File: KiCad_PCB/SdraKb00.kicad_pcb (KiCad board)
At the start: 2 copper layers, 85.3 x 83.4 mm, 75 parts, among them J1 AVR-ISP-6, SW00 SW_Push_45deg, SW01 SW_Push_45deg, SW02 SW_Push_45deg, SW03 RotaryEncoder_Switch, SW10 SW_Push_45deg, SW11 SW_Push_45deg, SW12 SW_Push_45deg, SW13 SW_Push_45deg, SW20 SW_Push_45deg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

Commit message: Finilizing PCB design.
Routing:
- net VCC: track 15.9 -> 20.6 mm
- net GND: track 108.5 -> 110.4 mm, vias 38 -> 40

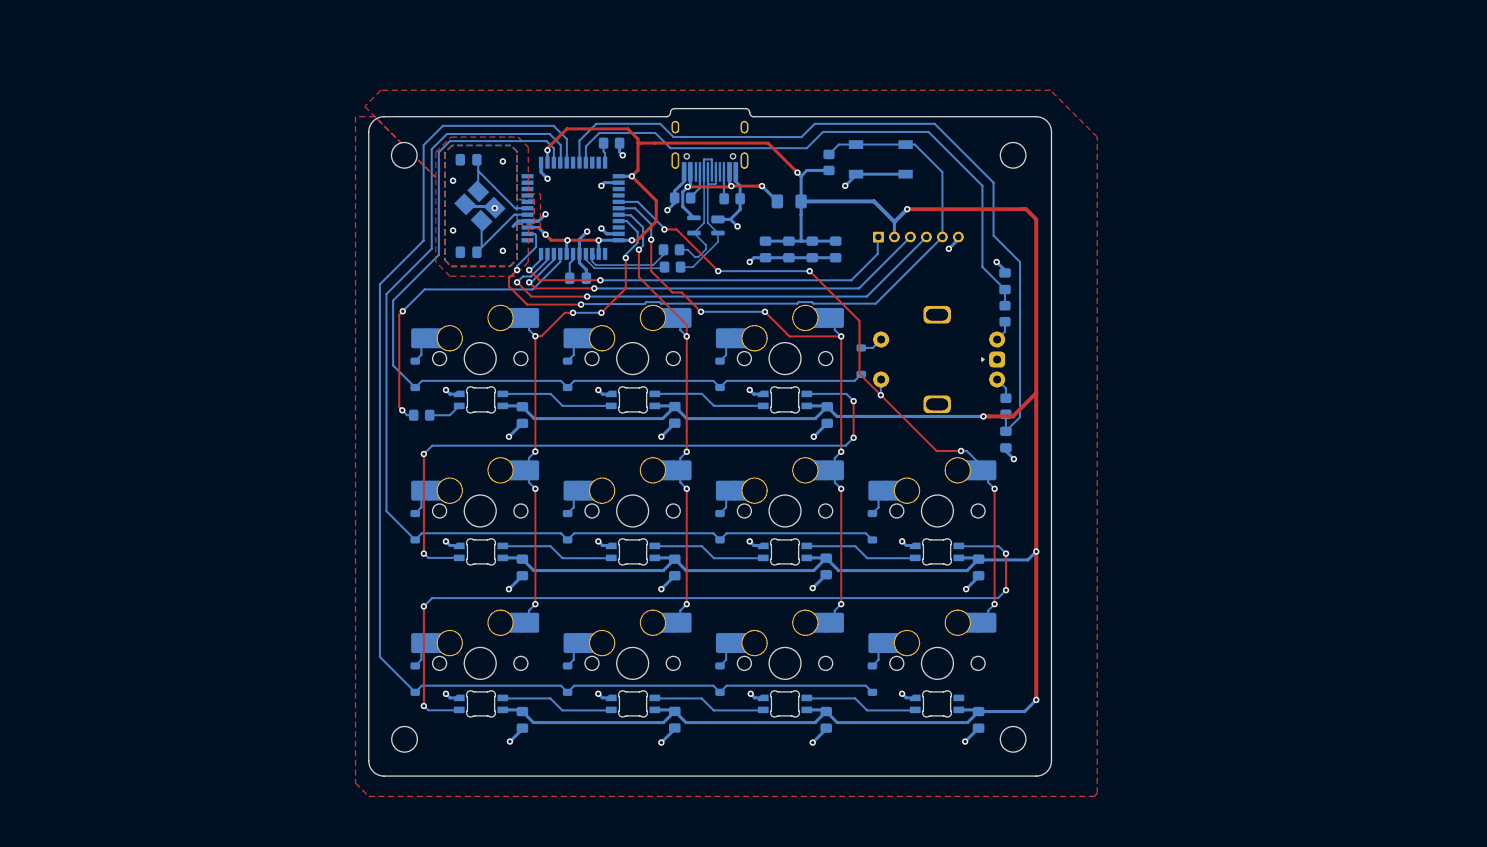
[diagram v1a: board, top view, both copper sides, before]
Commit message: Silkscreen (#5)
* Adding initial silkscreen.

* Adding KiCad & OpenHW logos.
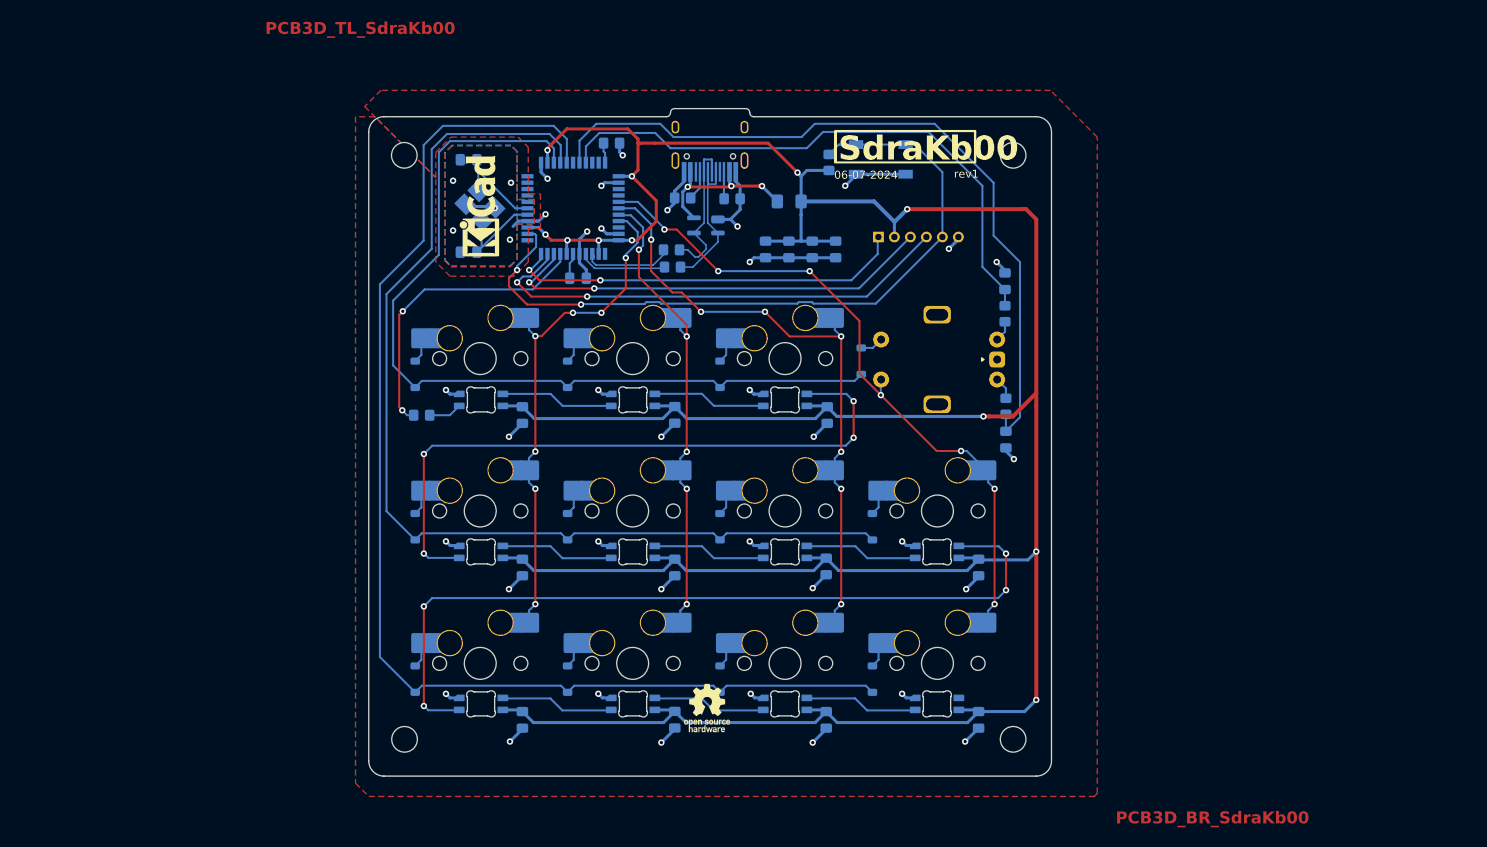
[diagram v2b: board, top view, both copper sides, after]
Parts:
- added REF**: KiCad-Logo_5mm_SilkScreen, Symbol:KiCad-Logo_5mm_SilkScreen, F.Cu at (115.4, 73.9)
- added REF**: OSHW-Logo_5.7x6mm_SilkScreen, Symbol:OSHW-Logo_5.7x6mm_SilkScreen, F.Cu at (143.4, 136.7)
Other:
- board text added: "06-07-2024"
- board text added: "PCB3D_BR_SdraKb00"
- board text added: "PCB3D_TL_SdraKb00"
- board text added: "SdraKb00"
- board text added: "rev1"

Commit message: Adding PCB renders.
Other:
- board text removed: "PCB3D_BR_SdraKb00"
- board text removed: "PCB3D_TL_SdraKb00"
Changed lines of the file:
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@@
 		(fp_arc
 			(start 1.749484 0.919719)
-			(mid 1.712541 0.814065)
+			(mid 1.712534 0.814065)
 			(end 1.699999 0.702841)
 			(stroke
@@
 		(fp_arc
 			(start 1.699999 -0.702844)
-			(mid 1.712538 -0.814067)
+			(mid 1.712537 -0.814067)
 			(end 1.749484 -0.919721)
 			(stroke
@@
 		(fp_arc
 			(start 1.749484 0.919719)
-			(mid 1.712534 0.814065)
+			(mid 1.712541 0.814065)
 			(end 1.699999 0.702841)
 			(stroke
@@
 		(fp_arc
 			(start 1.699999 -0.702844)
-			(mid 1.712537 -0.814067)
+			(mid 1.712538 -0.814067)
 			(end 1.749484 -0.919721)
 			(stroke
@@
 		(fp_arc
 			(start 1.749484 0.919719)
-			(mid 1.712541 0.814065)
+			(mid 1.712534 0.814065)
 			(end 1.699999 0.702841)
 			(stroke
@@
 		(fp_arc
 			(start 1.699999 -0.702844)
-			(mid 1.712538 -0.814067)
+			(mid 1.712537 -0.814067)
 			(end 1.749484 -0.919721)
 			(stroke
@@
 		(fp_arc
 			(start 1.749484 0.919719)
-			(mid 1.712534 0.814065)
+			(mid 1.712541 0.814065)
 			(end 1.699999 0.702841)
 			(stroke
@@
 		(fp_arc
 			(start 1.699999 -0.702844)
-			(mid 1.712537 -0.814067)
+			(mid 1.712538 -0.814067)
 			(end 1.749484 -0.919721)
 			(stroke
@@
 		(fp_arc
 			(start 1.749484 0.919719)
-			(mid 1.712541 0.814065)
+			(mid 1.712534 0.814065)
 			(end 1.699999 0.702841)
 			(stroke
@@
 		(fp_arc
 			(start 1.699999 -0.702844)
-			(mid 1.712538 -0.814067)
+			(mid 1.712537 -0.814067)
 			(end 1.749484 -0.919721)
 			(stroke
@@
 		(fp_arc
 			(start 1.749484 0.919719)
-			(mid 1.712541 0.814065)
+			(mid 1.712534 0.814065)
 			(end 1.699999 0.702841)
 			(stroke
@@
 		(fp_arc
 			(start 1.699999 -0.702844)
-			(mid 1.712538 -0.814067)
+			(mid 1.712537 -0.814067)
 			(end 1.749484 -0.919721)
 			(stroke
@@
 		(fp_arc
 			(start 1.749484 0.919719)
-			(mid 1.712541 0.814065)
+			(mid 1.712534 0.814065)
 			(end 1.699999 0.702841)
 			(stroke
@@
 		(fp_arc
 			(start 1.699999 -0.702844)
-			(mid 1.712538 -0.814067)
+			(mid 1.712537 -0.814067)
 			(end 1.749484 -0.919721)
 			(stroke
@@
 		(fp_arc
 			(start 1.749484 0.919719)
-			(mid 1.712541 0.814065)
+			(mid 1.712534 0.814065)
 			(end 1.699999 0.702841)
 			(stroke
@@
 		(fp_arc
 			(start 1.699999 -0.702844)
-			(mid 1.712538 -0.814067)
+			(mid 1.712537 -0.814067)
 			(end 1.749484 -0.919721)
 			(stroke
@@
 		(fp_arc
 			(start 1.749484 0.919719)
-			(mid 1.712534 0.814065)
+			(mid 1.712541 0.814065)
 			(end 1.699999 0.702841)
 			(stroke
@@
 		(fp_arc
 			(start 1.699999 -0.702844)
-			(mid 1.712537 -0.814067)
+			(mid 1.712538 -0.814067)
 			(end 1.749484 -0.919721)
 			(stroke
@@
 		(fp_arc
 			(start 1.749484 0.919719)
-			(mid 1.712541 0.814065)
+			(mid 1.712534 0.814065)
 			(end 1.699999 0.702841)
 			(stroke
@@
 		(fp_arc
 			(start 1.699999 -0.702844)
-			(mid 1.712538 -0.814067)
+			(mid 1.712537 -0.814067)
 			(end 1.749484 -0.919721)
 			(stroke
@@
 		(fp_arc
 			(start 1.749484 0.919719)
-			(mid 1.712541 0.814065)
+			(mid 1.712534 0.814065)
 			(end 1.699999 0.702841)
 			(stroke
@@
 		(fp_arc
 			(start 1.699999 -0.702844)
-			(mid 1.712538 -0.814067)
+			(mid 1.712537 -0.814067)
 			(end 1.749484 -0.919721)
 			(stroke
@@
 		(layer "Edge.Cuts")
 	)
-	(gr_text "PCB3D_BR_SdraKb00"
-		(at 194.437 151.257 0)
-		(layer "F.Cu")
-		(effects
-			(font
-				(size 1.5 1.5)
-				(thickness 0.3)
-				(bold yes)
-			)
-			(justify left bottom)
-		)
-	)
-	(gr_text "PCB3D_TL_SdraKb00"
-		(at 88.138 52.578 0)
-		(layer "F.Cu")
-		(effects
-			(font
-				(size 1.5 1.5)
-				(thickness 0.3)
-				(bold yes)
-			)
-			(justify left bottom)
-		)
-	)
 	(gr_text "SdraKb00"

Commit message: Adding power indicator LED (#7)
* Adding power indicator LED.

* Re-placing silkscreen.
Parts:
- removed the REF** at (115.4, 73.9)
- removed the REF** at (143.4, 136.7)
- added D4: RED 1.8V, LED_SMD:LED_1206_3216Metric_Pad1.42x1.75mm_HandSolder, F.Cu at (160.7, 67.1)
- added R10: 640, Resistor_SMD:R_0805_2012Metric_Pad1.20x1.40mm_HandSolder, F.Cu at (157.2, 66.5)
- added REF**: KiCad-Logo2_5mm_SilkScreen, Symbol:KiCad-Logo2_5mm_SilkScreen, F.Cu at (114.9, 73.8)
- added REF**: OSHW-Logo2_9.8x8mm_SilkScreen, Symbol:OSHW-Logo2_9.8x8mm_SilkScreen, F.Cu at (172.0, 68.1)
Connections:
- U1 pad 36: unconnected-(U1-PF7-Pad36) -> STATUS_LED
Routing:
- net +5V: track 418.6 -> 422.1 mm
- net Net-(D4-A): track 0.00 -> 3.44 mm

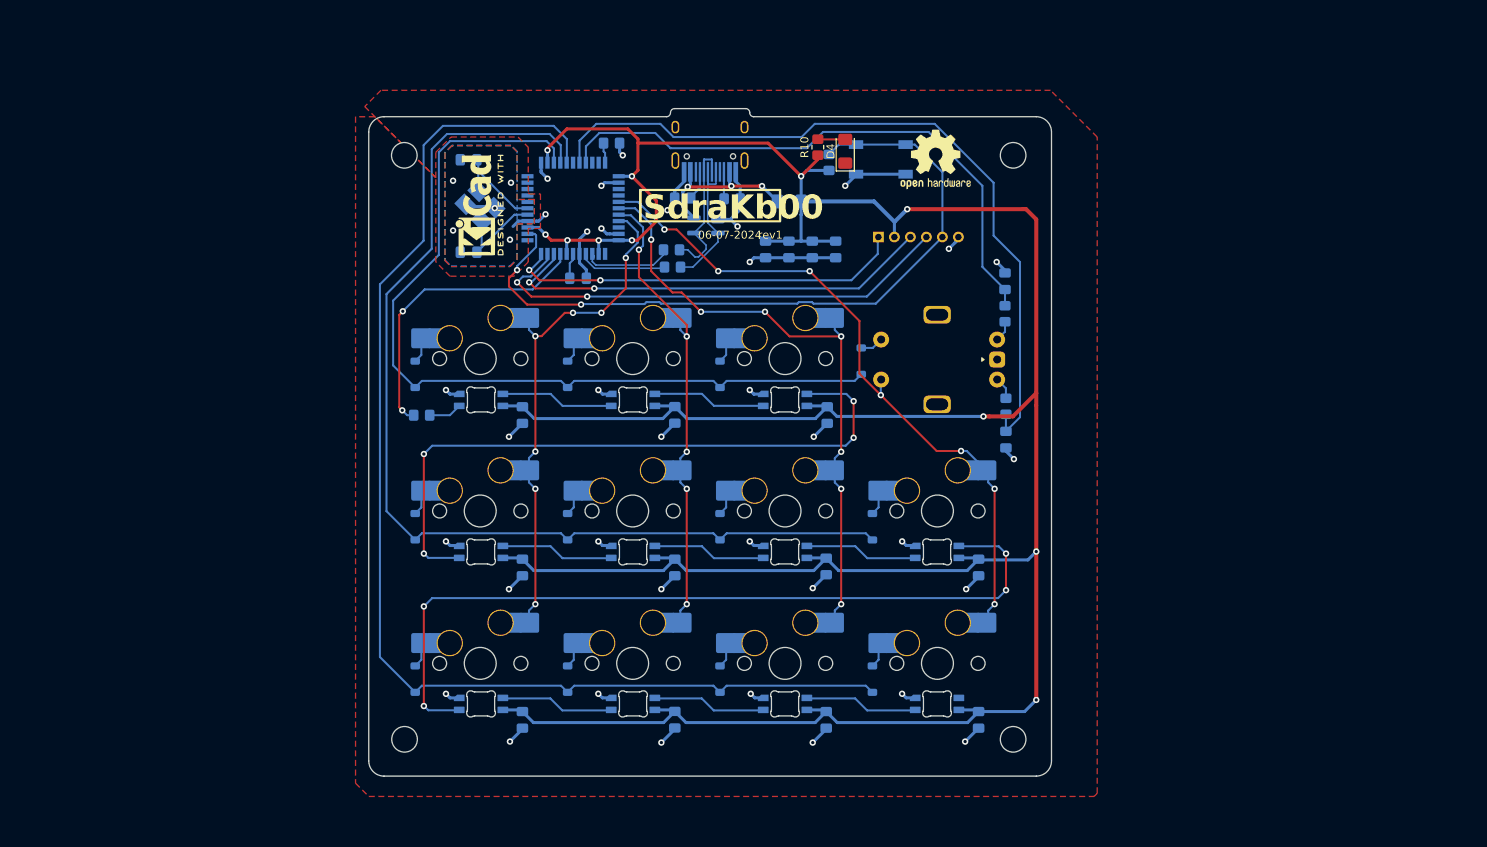
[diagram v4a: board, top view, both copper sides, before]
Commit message: Mounting plate (#8)
* Adding power indicator LED.

* Re-placing silkscreen.

* Adding switch mounting plate.
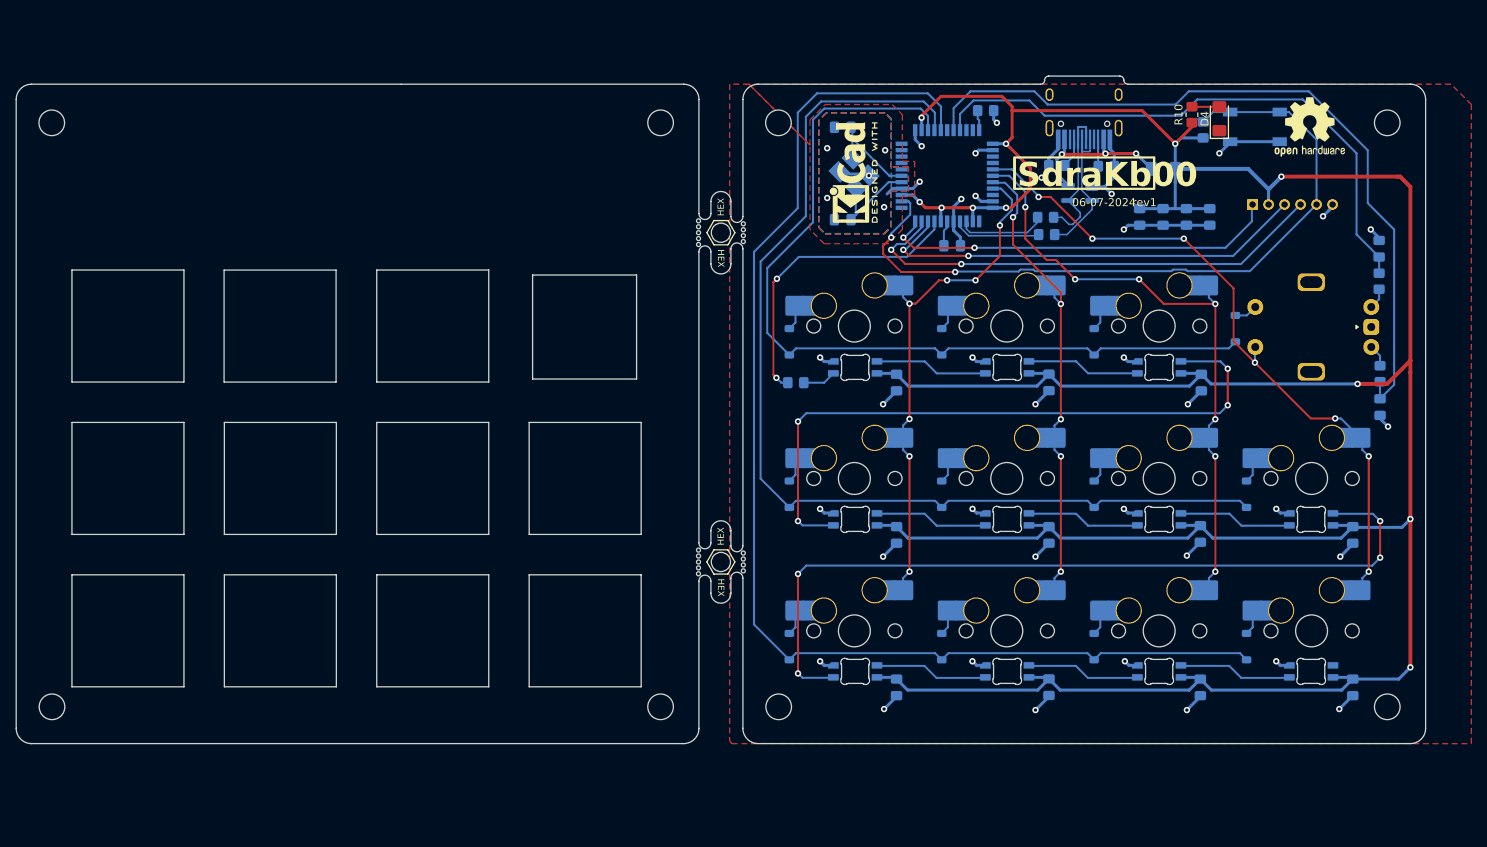
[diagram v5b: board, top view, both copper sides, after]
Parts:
- added H1: MountingHole, MountingHole:MountingHole_3.2mm_M3, F.Cu at (61.5, 136.5)
- added H2: MountingHole, MountingHole:MountingHole_3.2mm_M3, F.Cu at (137.6, 63.5)
- added H3: MountingHole, MountingHole:MountingHole_3.2mm_M3, F.Cu at (61.5, 63.5)
- added H4: MountingHole, MountingHole:MountingHole_3.2mm_M3, F.Cu at (137.6, 136.5)
- added MB5: 5.5mm, marbastlib-various:mousebites_5p5mm_easysnap, F.Cu at (147.9, 118.4)
- added MB5: 5.5mm, marbastlib-various:mousebites_5p5mm_easysnap, F.Cu at (147.9, 77.2)
- added SW01: SW_Push_45deg, marbastlib-mx:SW_MX_HS_CPG151101S11_1u, B.Cu at (90.0, 88.9)
- added SW01: SW_Push_45deg, marbastlib-mx:SW_MX_HS_CPG151101S11_1u, B.Cu at (71.0, 88.9)
- added SW01: SW_Push_45deg, marbastlib-mx:SW_MX_HS_CPG151101S11_1u, B.Cu at (90.0, 108.0)
- added SW01: SW_Push_45deg, marbastlib-mx:SW_MX_HS_CPG151101S11_1u, B.Cu at (71.0, 127.0)
- added SW01: SW_Push_45deg, marbastlib-mx:SW_MX_HS_CPG151101S11_1u, B.Cu at (109.1, 88.9)
- added SW01: SW_Push_45deg, marbastlib-mx:SW_MX_HS_CPG151101S11_1u, B.Cu at (109.1, 127.0)
- added SW01: SW_Push_45deg, marbastlib-mx:SW_MX_HS_CPG151101S11_1u, B.Cu at (128.1, 127.0)
- added SW01: SW_Push_45deg, marbastlib-mx:SW_MX_HS_CPG151101S11_1u, B.Cu at (109.1, 108.0)
- added SW01: SW_Push_45deg, marbastlib-mx:SW_MX_HS_CPG151101S11_1u, B.Cu at (71.0, 108.0)
- added SW01: SW_Push_45deg, marbastlib-mx:SW_MX_HS_CPG151101S11_1u, B.Cu at (90.0, 127.0)
- added SW01: SW_Push_45deg, marbastlib-mx:SW_MX_HS_CPG151101S11_1u, B.Cu at (128.1, 108.0)
- added SW03: RotaryEncoder_Switch, marbastlib-various:ROT_Alps_EC11E-Switch, F.Cu at (128.1, 89.0)
- moved C16 46.9 mm to (200.4, 75.3)
- moved C17 46.9 mm to (203.3, 75.3)
- moved C20 46.9 mm to (160.3, 64.1)
- moved C4 46.9 mm to (227.4, 79.2)
- moved C5 46.9 mm to (227.5, 99.0)
- moved Crgb02 46.9 mm to (205.2, 96.0)
- moved Crgb12 46.9 mm to (205.0, 114.9)
- moved Crgb13 46.9 mm to (224.1, 115.0)
- moved Crgb22 46.9 mm to (205.0, 134.1)
- moved Crgb23 46.9 mm to (224.1, 134.1)
- moved D13 46.9 mm to (210.8, 109.9)
- moved D23 46.9 mm to (210.8, 129.0)
- moved R2 46.9 mm to (227.4, 83.3)
- moved R3 46.9 mm to (227.5, 94.9)
- moved R4 46.9 mm to (178.2, 62.0)
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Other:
- board size 85.3 x 83.4 mm -> 176.2 x 83.4 mm
